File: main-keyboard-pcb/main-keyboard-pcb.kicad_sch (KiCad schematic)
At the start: 175 parts, among them J1 Debug SWD Connector, J2 Hotplug, J3 USB_B_Micro, SW1 SW_Push, SW10 SW_Push, SW11 SW_Push, SW12 SW_Push, SW13 SW_Push, SW14 SW_Push, SW15 SW_Push, SW16 SW_Push, SW17 SW_Push, SW18 SW_Push, SW19 SW_Push, SW2 SW_Push, SW20 SW_Push, SW21 SW_Push, SW22 SW_Push, SW23 SW_Push, SW24 SW_Push, SW25 SW_Push, SW26 SW_Push, SW27 SW_Push, SW28 SW_Push, SW29 SW_Push, SW3 SW_Push, SW30 SW_Push, SW31 SW_Push, SW32 SW_Push, SW33 SW_Push, SW34 SW_Push, SW35 SW_Push, SW36 SW_Push, SW37 SW_Push, SW38 SW_Push, SW39 SW_Push, SW4 SW_Push, SW40 SW_Push, SW41 SW_Push, SW42 SW_Push, SW43 SW_Push, SW44 SW_Push, SW45 SW_Push, SW46 SW_Push, SW47 SW_Push, SW48 SW_Push, SW49 SW_Push, SW5 SW_Push, SW50 SW_Push, SW51 SW_Push, SW52 SW_Push, SW53 SW_Push, SW54 SW_Push, SW55 SW_Push, SW56 SW_Push, SW57 SW_Push, SW58 SW_Push, SW59 SW_Push, SW6 SW_Push, SW60 SW_Push, SW61 SW_Push, SW62 SW_Push, SW63 SW_Push, SW64 SW_Push, SW65 SW_Push, SW66 SW_Push, SW67 SW_Push, SW7 SW_Push, SW8 SW_Push, SW9 SW_Push, SW99 SW_SPDT, U1 USBLC6-4SC6, U2 STM32F407VGT6, Y1 16MHz

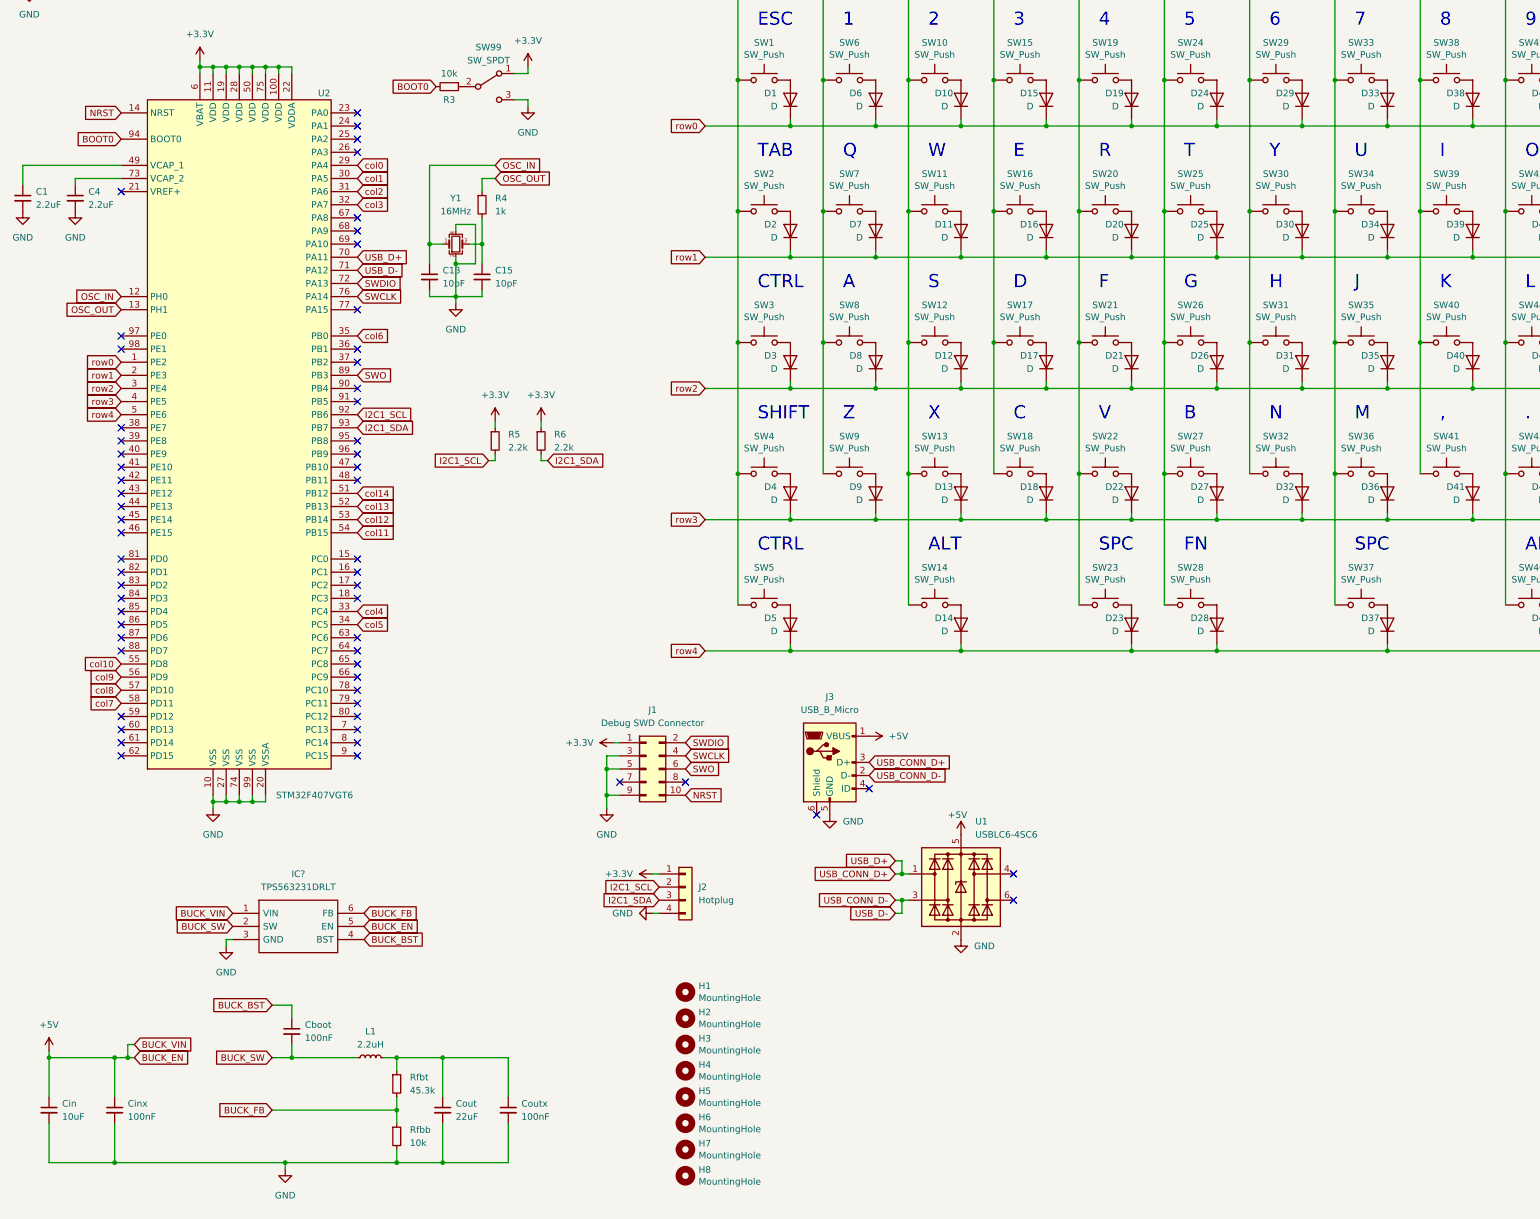
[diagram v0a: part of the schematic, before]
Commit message: Moved over components to 0805 packaging, updated buck converter, added side hotplug connector
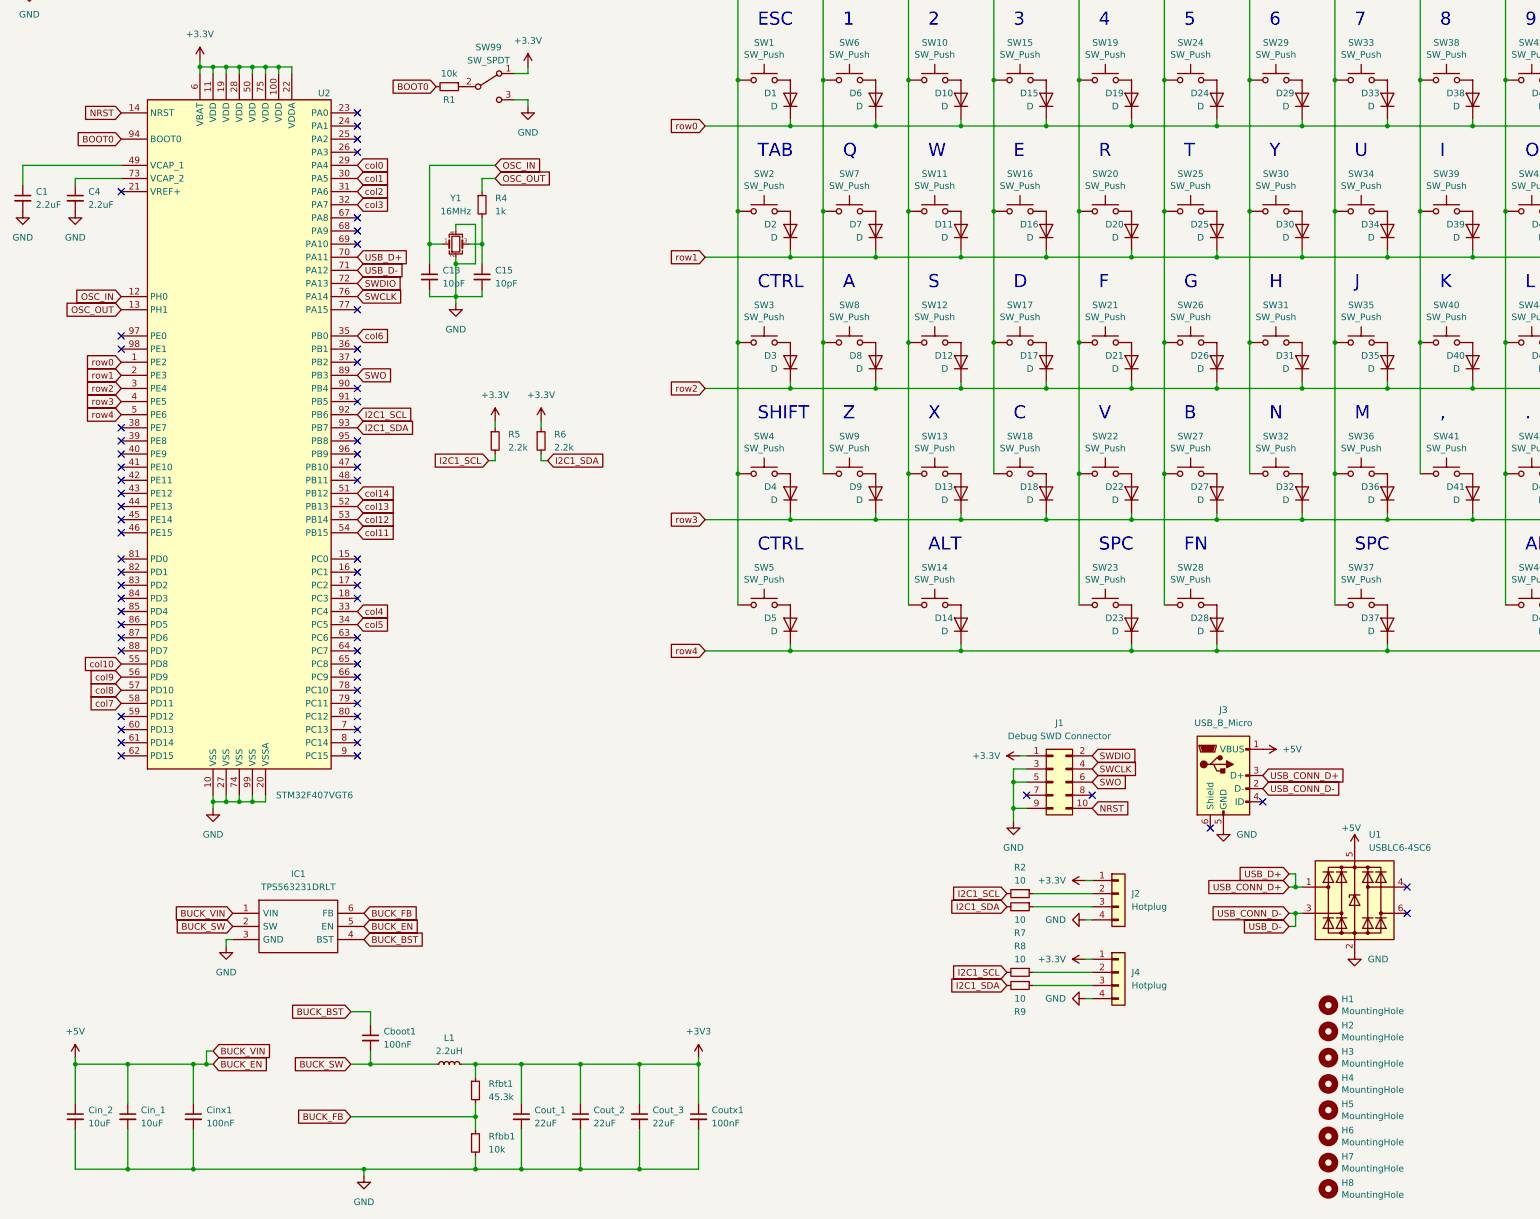
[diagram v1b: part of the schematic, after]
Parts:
- removed R3: 10k, stm32f4_2:ERJ-UP3F1002V, symbol Device:R_Small
- added Cin_2: 10uF, buck-converter:Cin, symbol Device:C_Small
- added Cout_2, Cout_3: 22uF, buck-converter:Cout, symbol Device:C_Small
- added J4: Hotplug, Connector_PinHeader_2.54mm:PinHeader_1x04_P2.54mm_Vertical, symbol Connector_Generic:Conn_01x04
- added R1: 10k, stm32f4_2:ERJ-U06F1002V, symbol Device:R_Small
- added R2, R7, R8, R9: 10, stm32f4_2:ERJ-U06J100V, symbol Device:R_Small
- Cboot1: renamed from Cboot; footprint (none) -> buck-converter:Cboot
- Cin_1: renamed from Cin; footprint (none) -> buck-converter:Cin
- Cinx1: renamed from Cinx; footprint (none) -> buck-converter:Cinx
- Cout_1: renamed from Cout; footprint (none) -> buck-converter:Cout
- Coutx1: renamed from Coutx; footprint (none) -> buck-converter:Coutx
- IC1: renamed from IC?; footprint TPS563231DRLT -> buck-converter:TPS563231DRLT
- J1: footprint Connector_PinHeader_1.27mm:PinHeader_2x05_P1.27mm_Vertical_SMD -> Connector_PinSocket_2.54mm:PinSocket_2x05_P2.54mm_Vertical
- L1: footprint (none) -> buck-converter:L1
- R4: footprint stm32f4_2:ERJ-UP3D1001V -> stm32f4_2:ERJ-U06F1001V
- R5, R6: footprint stm32f4_2:ERJ-UP3F2201V -> stm32f4_2:ERJ-U06F2201V
- Rfbb1: renamed from Rfbb; footprint (none) -> buck-converter:Rfbb
- Rfbt1: renamed from Rfbt; footprint (none) -> buck-converter:Rfbt
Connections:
- net +3V3: now also Cout_1.1, Coutx1.1, L1.2, Rfbt1.1, Cout_2.1, Cout_3.1, J4.1 (Pin_1)
- net +5V: now also Cin_2.1
- net BOOT0: now also R1.2
- net GND: now also Cin_2.2, Cout_2.2, Cout_3.2, J4.4 (Pin_4)
- net I2C1_SCL: now also R2.2, R8.2; no longer J2.2 (Pin_2)
- net I2C1_SDA: now also R7.2, R9.2; no longer J2.3 (Pin_3)
- net at SW99.2 (B): now also R1.1
- new net: J2.3 (Pin_3), R7.1
- new net: J4.2 (Pin_2), R8.1
- new net: J4.3 (Pin_3), R9.1
- new net: J2.2 (Pin_2), R2.1
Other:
- moved on the sheet: Cboot1, Cin_1, Cinx1, Cout_1, Coutx1, H1, H2, H3, H4, H5, H6, H7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

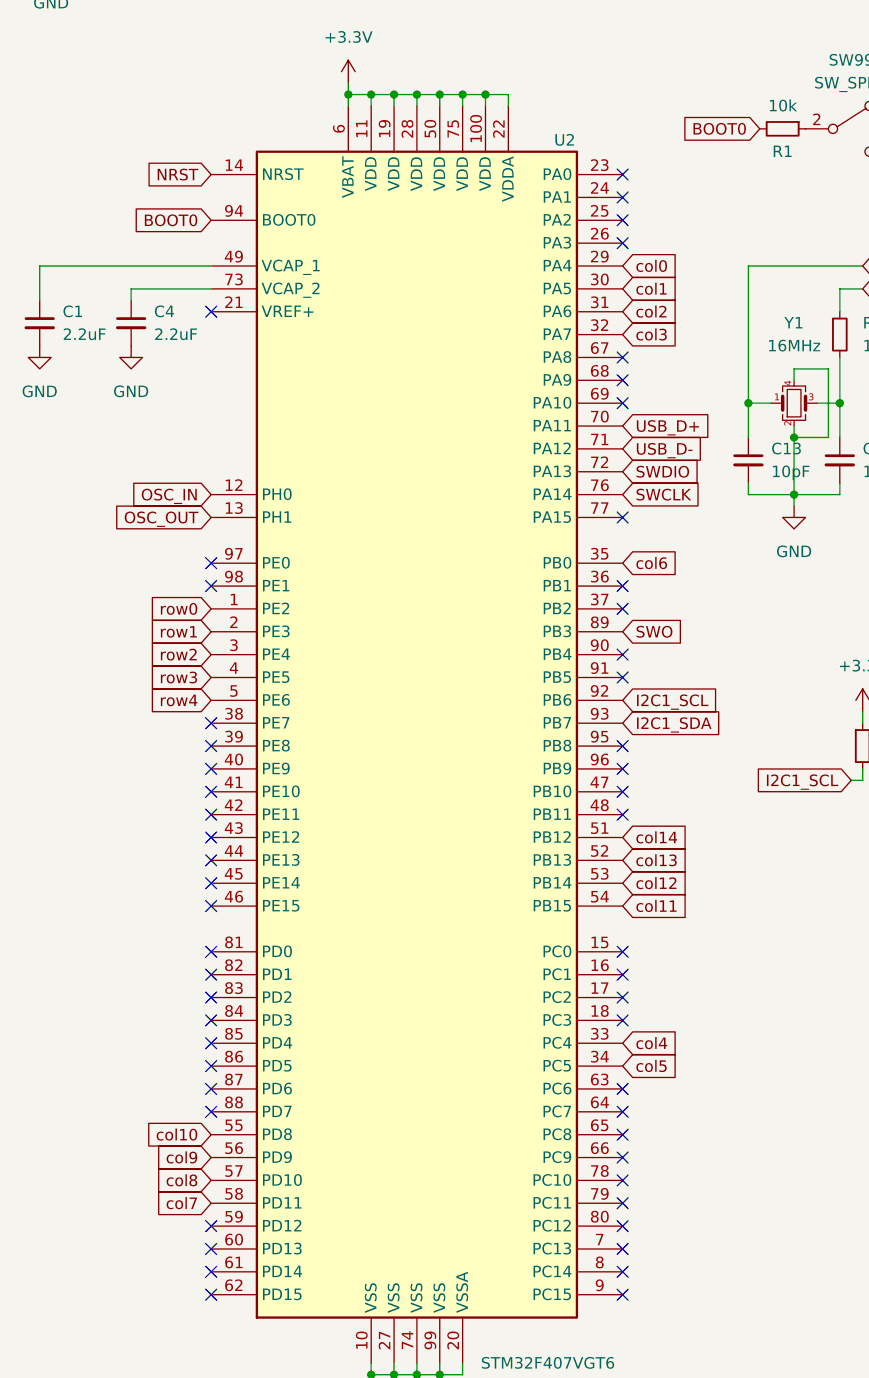
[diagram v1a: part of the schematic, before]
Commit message: moved cols to GPIOE and rows to GPIOA
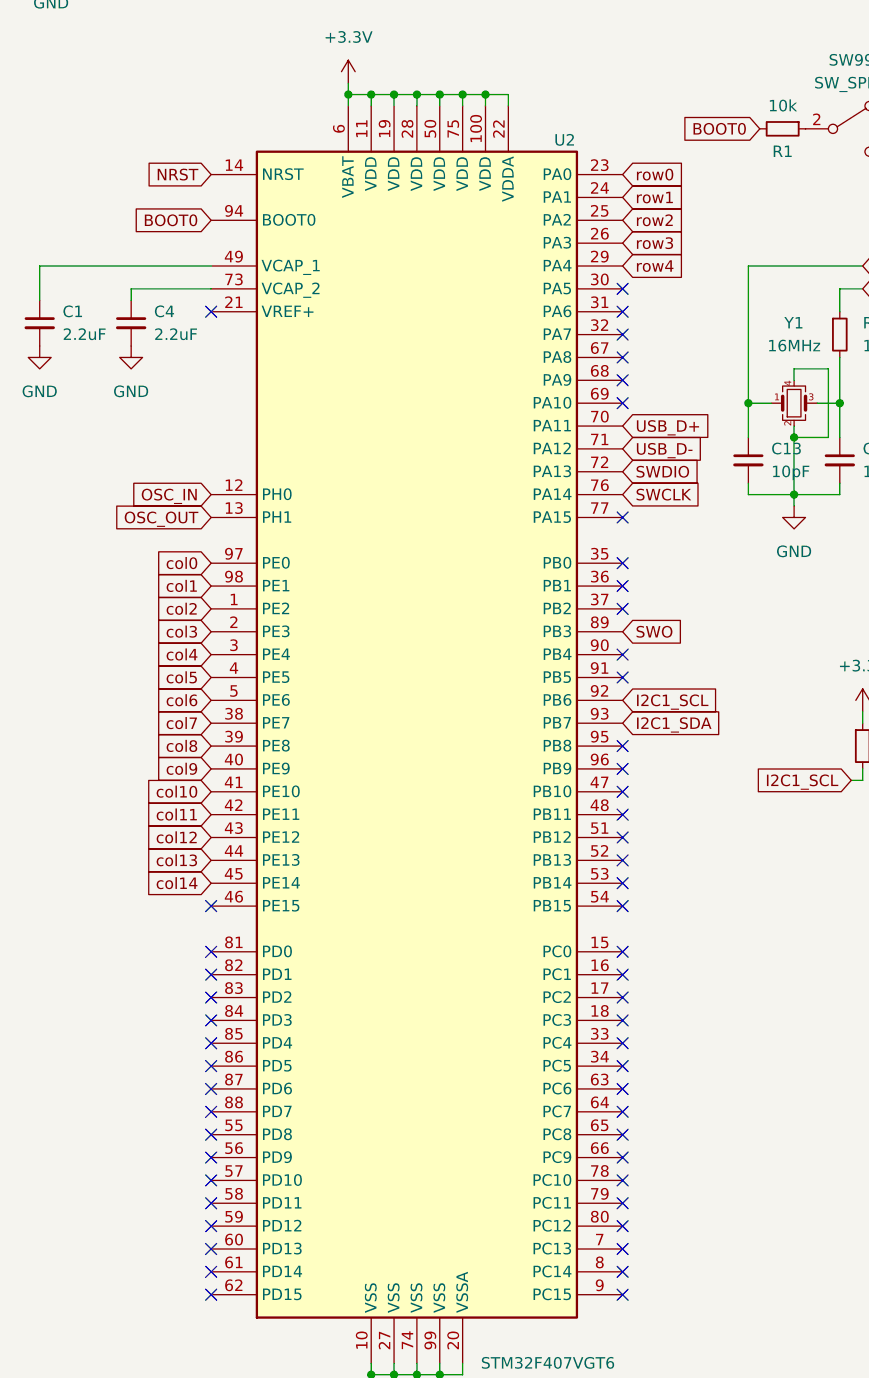
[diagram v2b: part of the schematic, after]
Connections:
- net col0: now also U2.97 (PE0); no longer U2.29 (PA4)
- net col1: now also U2.98 (PE1); no longer U2.30 (PA5)
- net col10: now also U2.41 (PE10); no longer U2.55 (PD8)
- net col11: now also U2.42 (PE11); no longer U2.54 (PB15)
- net col12: now also U2.43 (PE12); no longer U2.53 (PB14)
- net col13: now also U2.44 (PE13); no longer U2.52 (PB13)
- net col14: now also U2.45 (PE14); no longer U2.51 (PB12)
- net col2: now also U2.1 (PE2); no longer U2.31 (PA6)
- net col3: now also U2.2 (PE3); no longer U2.32 (PA7)
- net col4: now also U2.3 (PE4); no longer U2.33 (PC4)
- net col5: now also U2.4 (PE5); no longer U2.34 (PC5)
- net col6: now also U2.5 (PE6); no longer U2.35 (PB0)
- net col7: now also U2.38 (PE7); no longer U2.58 (PD11)
- net col8: now also U2.39 (PE8); no longer U2.57 (PD10)
- net col9: now also U2.40 (PE9); no longer U2.56 (PD9)
- net row0: now also U2.23 (PA0); no longer U2.1 (PE2)
- net row1: now also U2.24 (PA1); no longer U2.2 (PE3)
- net row2: now also U2.25 (PA2); no longer U2.3 (PE4)
- net row3: now also U2.26 (PA3); no longer U2.4 (PE5)
- net row4: now also U2.29 (PA4); no longer U2.5 (PE6)
